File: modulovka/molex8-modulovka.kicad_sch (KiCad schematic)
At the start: 7 parts, among them J1 Conn_01x04, J2 Conn_02x04_Counter_Clockwise, J3 Conn_01x04

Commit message: Customize modulovka pcb.
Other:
- title: MOLEX to screw-terminals PCB -> MOLEX to screw-terminals PCB for modules connection
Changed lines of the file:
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@@
   (paper "A5")
   (title_block
-    (title "MOLEX to screw-terminals PCB")
+    (title "MOLEX to screw-terminals PCB for modules connection")
     (date "2022-12-02")
     (rev "1.0")
+    (comment 4 "Silkscreen texts added compared to plain molex8 pcb.")
   )
   (wire (pts (xy 106.68 57.15) (xy 120.65 57.15))

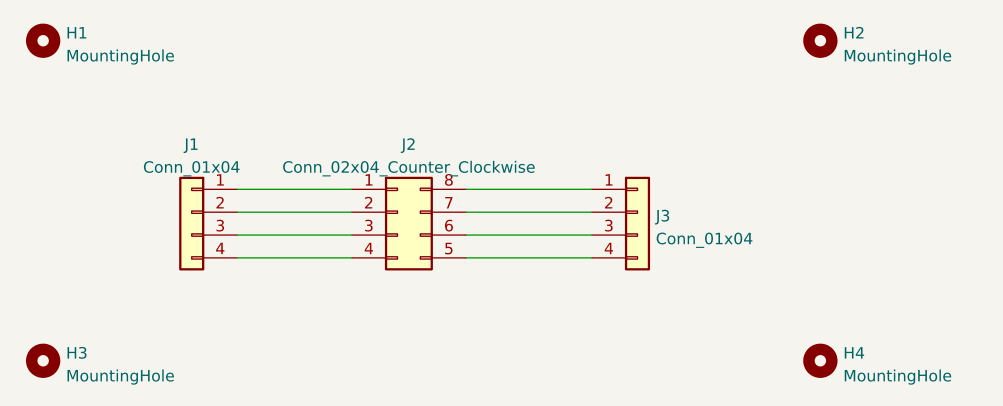
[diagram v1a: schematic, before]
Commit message: Use screw terminal symbols, use MVE25-5-V as values.
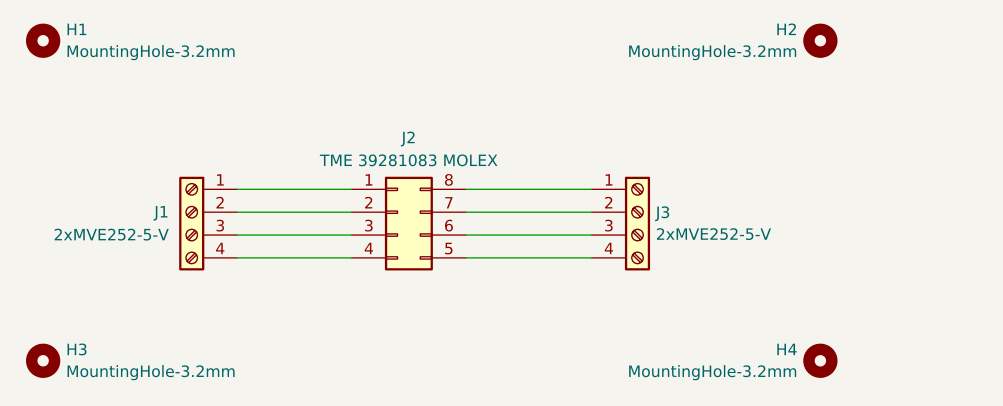
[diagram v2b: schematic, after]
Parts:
- H1, H2, H3, H4: value MountingHole -> MountingHole-3.2mm
- J1, J3: value Conn_01x04 -> 2xMVE252-5-V; symbol Connector_Generic:Conn_01x04 -> Connector:Screw_Terminal_01x04
- J2: value Conn_02x04_Counter_Clockwise -> TME 39281083 MOLEX
